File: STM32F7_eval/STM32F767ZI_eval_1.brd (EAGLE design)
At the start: 76.2 x 53.3 mm, 92 parts, among them CN1 GROVE-4P-CONN-I2C-90D, CN2 GROVE-4P-CONN-I2C-90D, CN3 GROVE-4P-CONN-I2C-90D, CN4 GROVE-4P-CONN-AN01-90D, CN5 ARDUINO_COMPAT_IF, CN6 STLINKV21_SWD_IF, CN7 WFT0750CZ09-SMD_, CN8 MCO_IF, CN9 UART_IF, Q1 PMF370XN_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

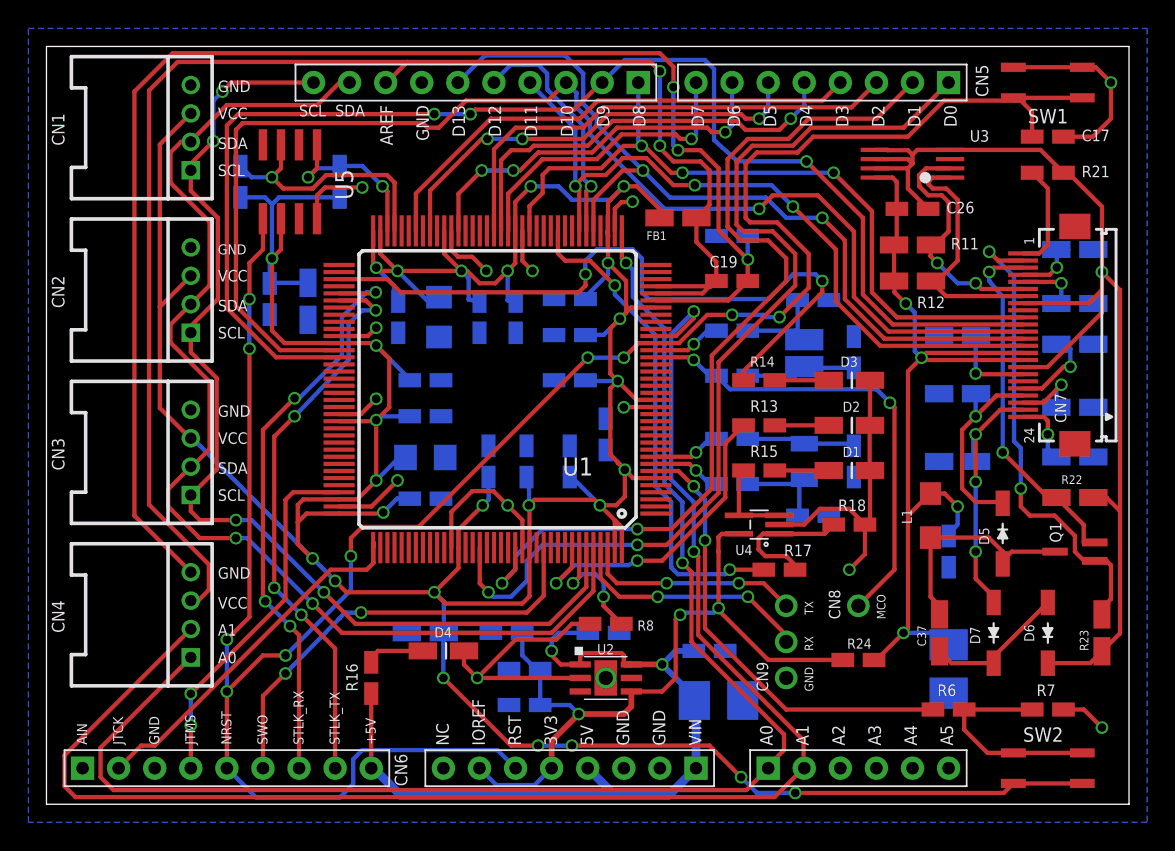
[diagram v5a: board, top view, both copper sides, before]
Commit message: 評価回路を修正
・デバイス追加に伴い、配線パターンを大幅に変更
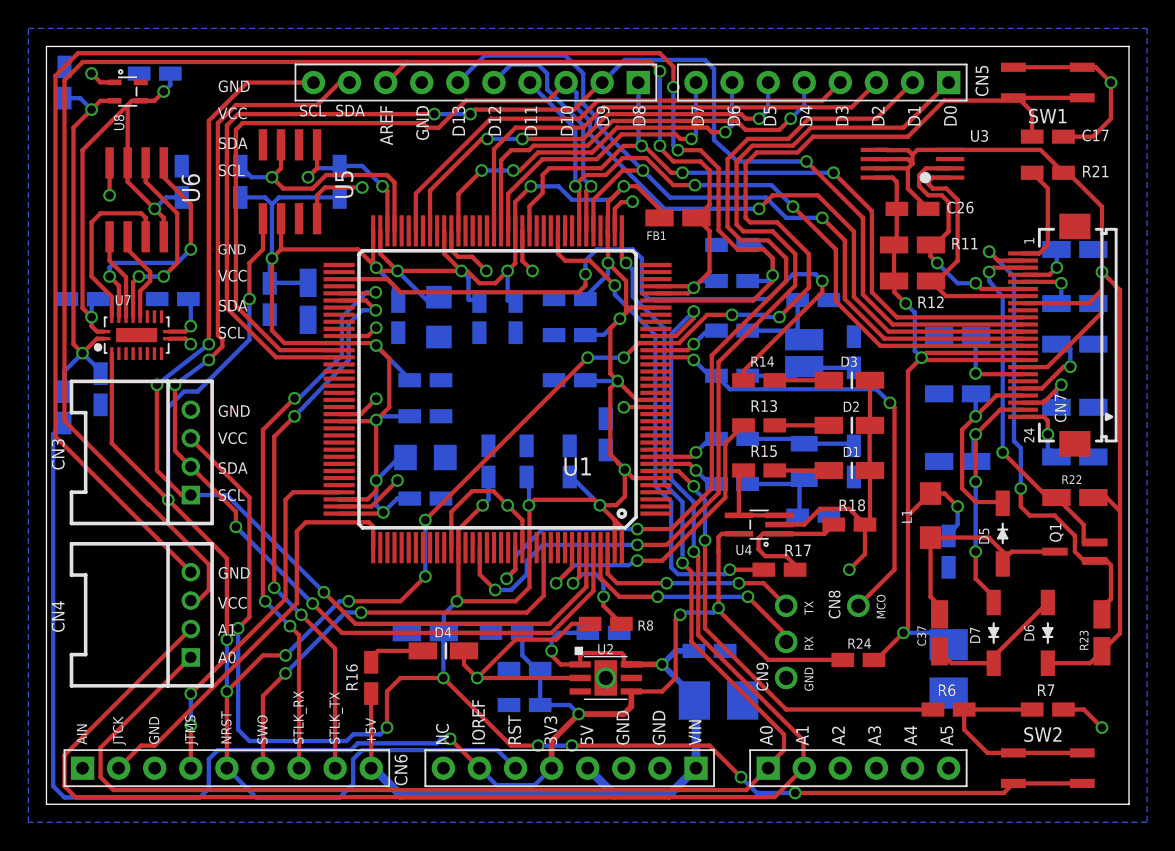
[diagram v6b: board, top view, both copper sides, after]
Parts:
- removed CN1, CN2: GROVE-4P-CONN-I2C-90D, PartsForProto:GROVE-4P-90D
- added C42, C44, C45, C46: 0.1uF, Parts:SMD_1608_DEV
- added C43: 1uF, Parts:SMD_1608_DEV
- added R25: 0, Parts:SMD_1608_DEV
- added R5: 10k, Parts:SMD_1608_DEV
- added U6: MX25U6435F, Parts:SO8
- added U7: FXMA108, Parts:DQFN20
- added U8: NCP563, Parts:SC-70-4
- moved R9 0.64 mm to (48.3, 39.4)
- flipped C19 to the bottom, turned to 180 degrees
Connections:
- new net !CS!: U6.1, U7.18
- new net !RESET!: U6.7, U7.19
- new net +18V: C42.1, C44.1, C46.1, U6.3, U6.8, U7.20, U8.3
- new net N$15: R5.2, U7.11
- new net PA15: U1.110, U7.3
- new net PC10: U1.111, U7.6
- new net PC11: U1.112, U7.5
- new net PC12: U1.113, U7.4
- new net SCLK: U6.6, U7.15
- new net SI: U6.5, U7.17
- new net SO: U6.2, U7.16
- new net VCC_MEM: C43.1, C45.1, R25.2, U7.1, U8.2
- net +3V3: now also R25.1
- net 0V: now also C42.2, C43.2, C44.2, C45.2, C46.2, R5.1, U6.4, U7.10, U8.1; no longer CN1.4, CN2.4
- net NRST: now also U7.2
- net PB8: no longer CN1.1, CN2.1
- net PB9: no longer CN1.2, CN2.2
- net VDD: no longer CN1.3, CN2.3
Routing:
- net +3V3: track 53.3 -> 113.3 mm, vias 3 -> 4
- net +18V: track 0.00 -> 36.6 mm, vias 0 -> 3
- net VCC_MEM: track 0.00 -> 29.2 mm, vias 0 -> 2
- net !CS!: track 0.00 -> 16.9 mm, vias 0 -> 2
- net NRST: track 159.7 -> 175.8 mm, vias 10 -> 12
- net AGND: track 101.8 -> 117.5 mm
- net SO: track 0.00 -> 14.1 mm, vias 0 -> 2
- net !RESET!: track 0.00 -> 12.8 mm
- net VDD: track 315.8 -> 305.0 mm
- net AVDD: track 104.3 -> 112.9 mm, vias 2 -> 3
- net PB9: track 82.1 -> 74.9 mm, vias 2 -> 4
- net SCLK: track 0.00 -> 6.57 mm
- net SI: track 0.00 -> 6.10 mm
- net 0V: track 179.9 -> 185.7 mm, vias 15 -> 18
- net TCK: track 25.8 -> 29.7 mm
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
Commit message: 評価回路を修正
・VCAP_1、VCAP_2の配線が間違っていたので修正
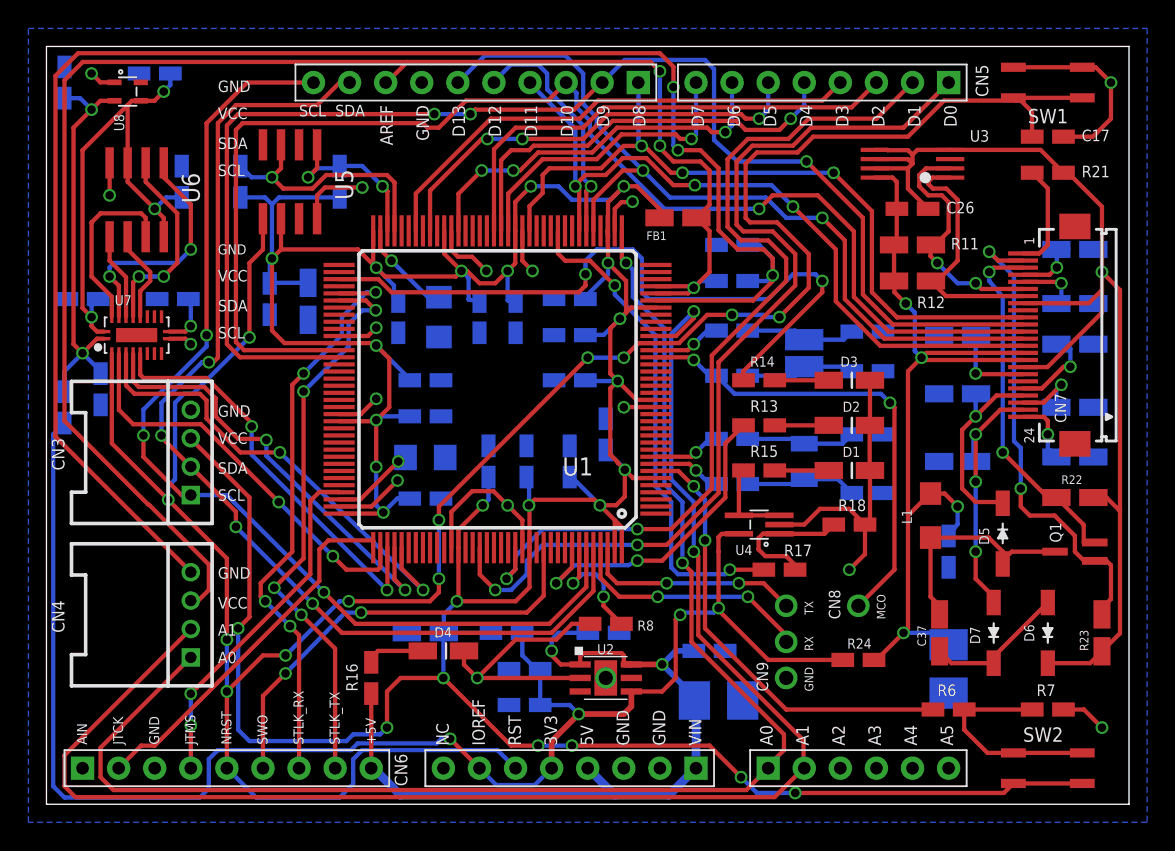
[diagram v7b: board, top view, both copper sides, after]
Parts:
- moved C15 4.41 mm to (57.8, 33.3)
- moved C14 4.13 mm to (57.8, 21.9)
- moved C13 2.13 mm to (57.8, 26.0), turned to 180 degrees
- moved C16 1.64 mm to (57.8, 30.5), turned to 180 degrees
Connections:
- new net VCAP_1: C20.1, U1.71
- new net VCAP_2: C21.1, U1.106
- net VDD: no longer C20.1, C21.1, U1.106, U1.71
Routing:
- net PC12: track 0.00 -> 33.3 mm, vias 0 -> 2
- net PC11: track 0.00 -> 31.8 mm, vias 0 -> 2
- net PC10: track 0.00 -> 29.4 mm, vias 0 -> 2
- net PA15: track 0.00 -> 28.5 mm, vias 0 -> 2
- net VDD: track 305.0 -> 290.2 mm, vias 26 -> 25
- net VCAP_1: track 0.00 -> 6.83 mm, vias 0 -> 1
- net VCAP_2: track 0.00 -> 5.89 mm, vias 0 -> 1
- net TCK: track 29.7 -> 26.4 mm
- net PD15: track 93.9 -> 95.4 mm
- net PD14: track 89.9 -> 91.4 mm
- net N$2: track 6.40 -> 7.87 mm
- net TMS: track 25.6 -> 24.6 mm
- net NRST: track 175.8 -> 176.8 mm
- net PB9: track 74.9 -> 75.7 mm
- net N$1: track 7.23 -> 7.83 mm
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
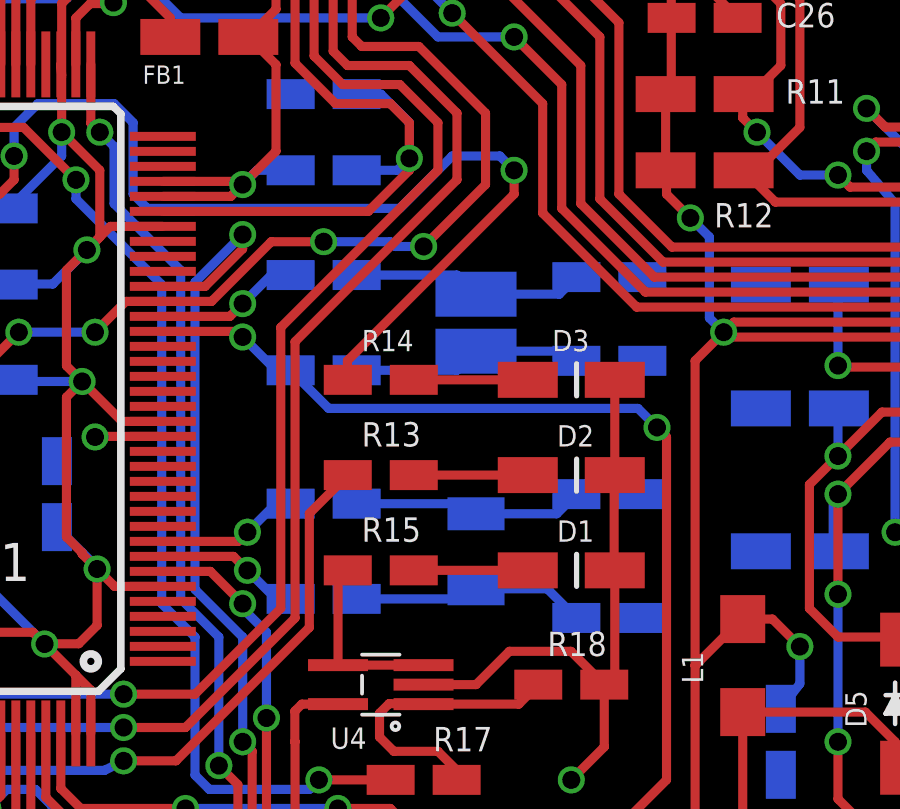
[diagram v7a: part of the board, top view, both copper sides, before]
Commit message: 評価回路を修正
・手はんだパターンに修正
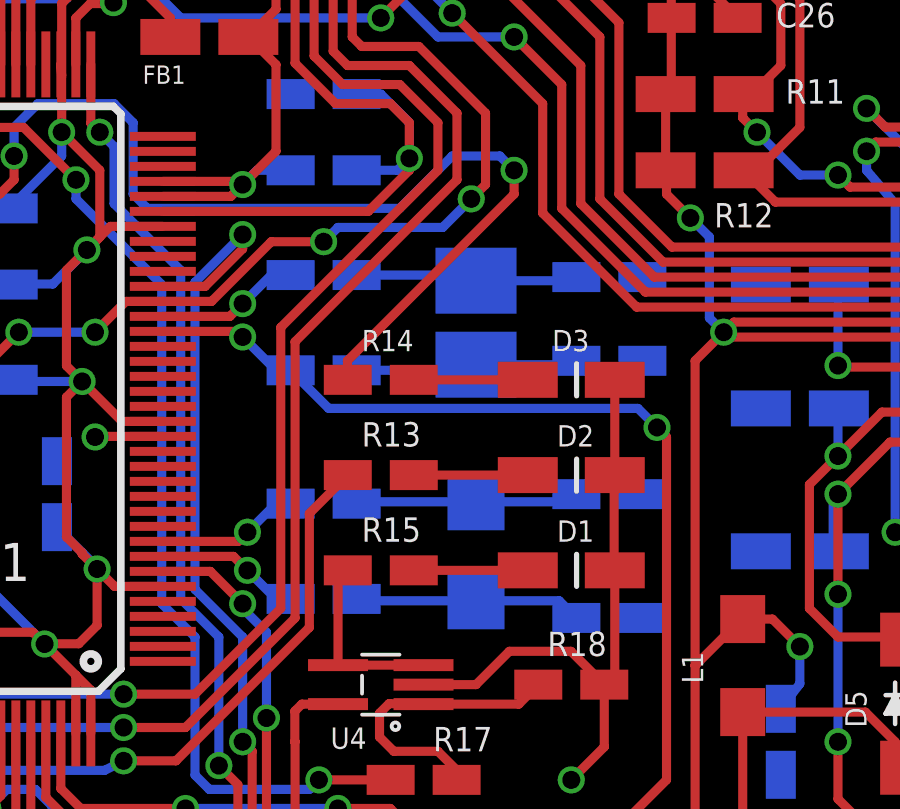
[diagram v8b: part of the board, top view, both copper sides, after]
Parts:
- X1: value NX3215SA-32.768K -> NX3215SA_; device Parts:NX3215 -> Parts:NX3215_DEV
- X2: value NX3225GD-8MHZ -> NX3225GD_; device Parts:NX3225 -> Parts:NX3225_DEV
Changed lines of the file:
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@@
 <setting verticaltext="up"/>
 </settings>
-<grid distance="50" unitdist="mil" unit="mil" style="lines" multiple="1" display="yes" altdistance="0.025" altunitdist="inch" altunit="inch"/>
+<grid distance="0.05" unitdist="inch" unit="mil" style="lines" multiple="1" display="yes" altdistance="0.025" altunitdist="inch" altunit="inch"/>
 <layers>
 <layer number="1" name="Top" color="4" fill="1" visible="yes" active="yes"/>
@@
 </element>
 <element name="U1" library="Parts" package="LQFP144_DEV" value="STM32F767ZI_" x="31.75" y="29.21" rot="R180"/>
-<element name="X1" library="Parts" package="NX3215" value="NX3215SA-32.768K" x="53.34" y="24.13" smashed="yes" rot="MR270">
-<attribute name="NAME" x="52.115" y="26.2725" size="0.8128" layer="26" rot="MR90"/>
+<element name="X1" library="Parts" package="NX3215_DEV" value="NX3215SA_" x="53.34" y="24.13" smashed="yes" rot="MR270">
+<attribute name="NAME" x="51.1625" y="23.57375" size="0.8128" layer="26" rot="MR90"/>
 <attribute name="VALUE" x="55.39" y="25.955" size="0.8128" layer="28" rot="MR270"/>
 </element>
-<element name="X2" library="Parts" package="NX3225" value="NX3225GD-8MHZ" x="53.34" y="31.75" smashed="yes" rot="MR270">
-<attribute name="NAME" x="54.89" y="29.4475" size="0.8128" layer="26" rot="MR270"/>
+<element name="X2" library="Parts" package="NX3225_DEV" value="NX3225GD_" x="53.34" y="31.75" smashed="yes" rot="MR270">
+<attribute name="NAME" x="51.3975" y="32.305" size="0.8128" layer="26" rot="MR270"/>
 <attribute name="VALUE" x="55.79" y="33.575" size="0.8128" layer="28" rot="MR270"/>
 </element>
@@
 <contactref element="X1" pad="2"/>
 <contactref element="R2" pad="1"/>
-<wire x1="49.36" y1="22.5425" x2="53.0025" y2="22.5425" width="0.3048" layer="16"/>
-<wire x1="53.0025" y1="22.5425" x2="53.34" y2="22.88" width="0.3048" layer="16"/>
-<wire x1="53.34" y1="22.88" x2="55.7125" y2="22.88" width="0.3048" layer="16"/>
-<wire x1="55.7125" y1="22.88" x2="56.685" y2="21.9075" width="0.3048" layer="16"/>
+<wire x1="53.34" y1="22.48" x2="49.4225" y2="22.48" width="0.3048" layer="16"/>
+<wire x1="49.4225" y1="22.48" x2="49.36" y2="22.5425" width="0.3048" layer="16"/>
+<wire x1="53.34" y1="22.48" x2="56.1125" y2="22.48" width="0.3048" layer="16"/>
+<wire x1="56.1125" y1="22.48" x2="56.685" y2="21.9075" width="0.3048" layer="16"/>
 </signal>
 <signal name="N$3">
@@
 <contactref element="C13" pad="1"/>
 <contactref element="R1" pad="1"/>
-<wire x1="49.36" y1="25.7175" x2="53.0025" y2="25.7175" width="0.3048" layer="16"/>
-<wire x1="53.0025" y1="25.7175" x2="53.34" y2="25.38" width="0.3048" layer="16"/>
-<wire x1="53.34" y1="25.38" x2="56.03" y2="25.38" width="0.3048" layer="16"/>
-<wire x1="56.03" y1="25.38" x2="56.685" y2="26.035" width="0.3048" layer="16"/>
+<wire x1="53.34" y1="25.78" x2="49.4225" y2="25.78" width="0.3048" layer="16"/>
+<wire x1="49.4225" y1="25.78" x2="49.36" y2="25.7175" width="0.3048" layer="16"/>
+<wire x1="53.34" y1="25.78" x2="56.43" y2="25.78" width="0.3048" layer="16"/>
+<wire x1="56.43" y1="25.78" x2="56.685" y2="26.035" width="0.3048" layer="16"/>
 </signal>
 <signal name="N$1">
@@
 <contactref element="C15" pad="1"/>
 <contactref element="X2" pad="1"/>
-<wire x1="49.36" y1="33.3375" x2="52.7025" y2="33.3375" width="0.3048" layer="16"/>
-<wire x1="52.7025" y1="33.3375" x2="53.34" y2="32.7" width="0.3048" layer="16"/>
-<wire x1="53.34" y1="32.7" x2="56.115" y2="32.7" width="0.3048" layer="16"/>
-<wire x1="56.115" y1="32.7" x2="56.685" y2="33.27" width="0.3048" layer="16"/>
+<wire x1="53.34" y1="33.15" x2="56.565" y2="33.15" width="0.3048" layer="16"/>
+<wire x1="56.565" y1="33.15" x2="56.685" y2="33.27" width="0.3048" layer="16"/>
+<wire x1="49.36" y1="33.3375" x2="53.1525" y2="33.3375" width="0.3048" layer="16"/>
+<wire x1="53.1525" y1="33.3375" x2="53.34" y2="33.15" width="0.3048" layer="16"/>
 </signal>
 <signal name="N$5">
@@
 <contactref element="R4" pad="1"/>
 <contactref element="X2" pad="2"/>
-<wire x1="49.36" y1="30.1625" x2="52.7025" y2="30.1625" width="0.3048" layer="16"/>
-<wire x1="52.7025" y1="30.1625" x2="53.34" y2="30.8" width="0.3048" layer="16"/>
-<wire x1="53.34" y1="30.8" x2="56.365" y2="30.8" width="0.3048" layer="16"/>
-<wire x1="56.365" y1="30.8" x2="56.685" y2="30.48" width="0.3048" layer="16"/>
+<wire x1="53.34" y1="30.35" x2="56.555" y2="30.35" width="0.3048" layer="16"/>
+<wire x1="56.555" y1="30.35" x2="56.685" y2="30.48" width="0.3048" layer="16"/>
+<wire x1="49.36" y1="30.1625" x2="53.1525" y2="30.1625" width="0.3048" layer="16"/>
+<wire x1="53.1525" y1="30.1625" x2="53.34" y2="30.35" width="0.3048" layer="16"/>
 </signal>
 <signal name="PH1">
@@
 <via x="21.2725" y="14.2875" extent="1-16" drill="0.6"/>
 <wire x1="72.91" y1="49.725" x2="68.06" y2="49.725" width="0.3048" layer="1"/>
-<via x="51.59375" y="34.29" extent="1-16" drill="0.6"/>
+<via x="53.18125" y="35.8775" extent="1-16" drill="0.6"/>
 <wire x1="53.6575" y1="38.735" x2="51.435" y2="40.9575" width="0.3048" layer="1"/>
 <wire x1="51.435" y1="40.9575" x2="49.53" y2="40.9575" width="0.3048" layer="1"/>
@@
 <wire x1="15.24" y1="10.4775" x2="12.7" y2="7.9375" width="0.3048" layer="1"/>
 <wire x1="53.6575" y1="38.735" x2="53.6575" y2="36.35375" width="0.3048" layer="1"/>
-<wire x1="53.6575" y1="36.35375" x2="51.59375" y2="34.29" width="0.3048" layer="1"/>
-<wire x1="51.59375" y1="34.29" x2="50.64125" y2="34.29" width="0.3048" layer="16"/>
-<wire x1="50.64125" y1="34.29" x2="50.4825" y2="34.44875" width="0.3048" layer="16"/>
-<wire x1="50.4825" y1="34.44875" x2="48.26" y2="34.44875" width="0.3048" layer="16"/>
 <contactref element="U5" pad="1"/>
 <wire x1="15.24" y1="41.215" x2="15.24" y2="39.0525" width="0.3048" layer="1"/>
@@
 <wire x1="26.9875" y1="14.2875" x2="27.6225" y2="14.9225" width="0.3048" layer="1"/>
 <wire x1="27.6225" y1="14.9225" x2="27.6225" y2="15.875" width="0.3048" layer="1"/>
+<wire x1="52.22875" y1="34.925" x2="53.18125" y2="35.8775" width="0.3048" layer="16"/>
+<wire x1="52.22875" y1="34.925" x2="48.73625" y2="34.925" width="0.3048" layer="16"/>
+<wire x1="48.73625" y1="34.925" x2="48.26" y2="34.44875" width="0.3048" layer="16"/>
+<wire x1="53.18125" y1="35.8775" x2="53.6575" y2="36.35375" width="0.3048" layer="1"/>
 </signal>
 <signal name="SWO">
